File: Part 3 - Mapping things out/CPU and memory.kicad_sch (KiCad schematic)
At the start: 6 parts

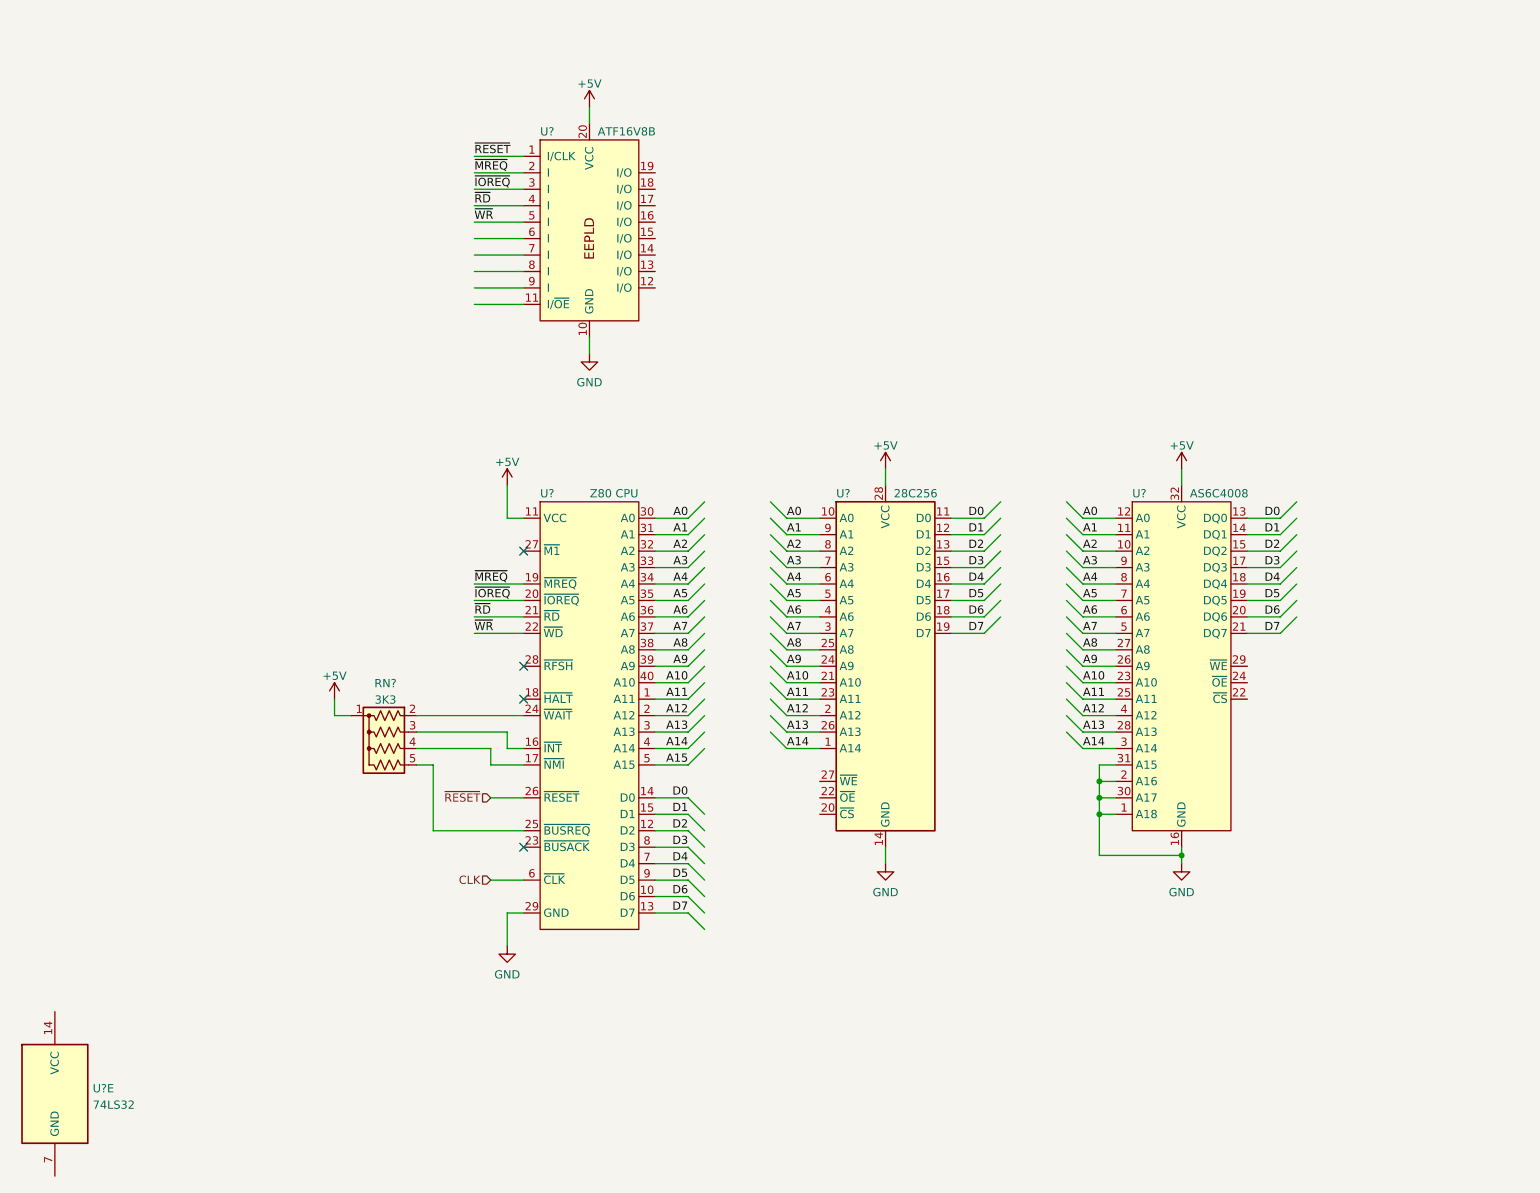
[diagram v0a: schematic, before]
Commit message: Updated glue logic and bank switching
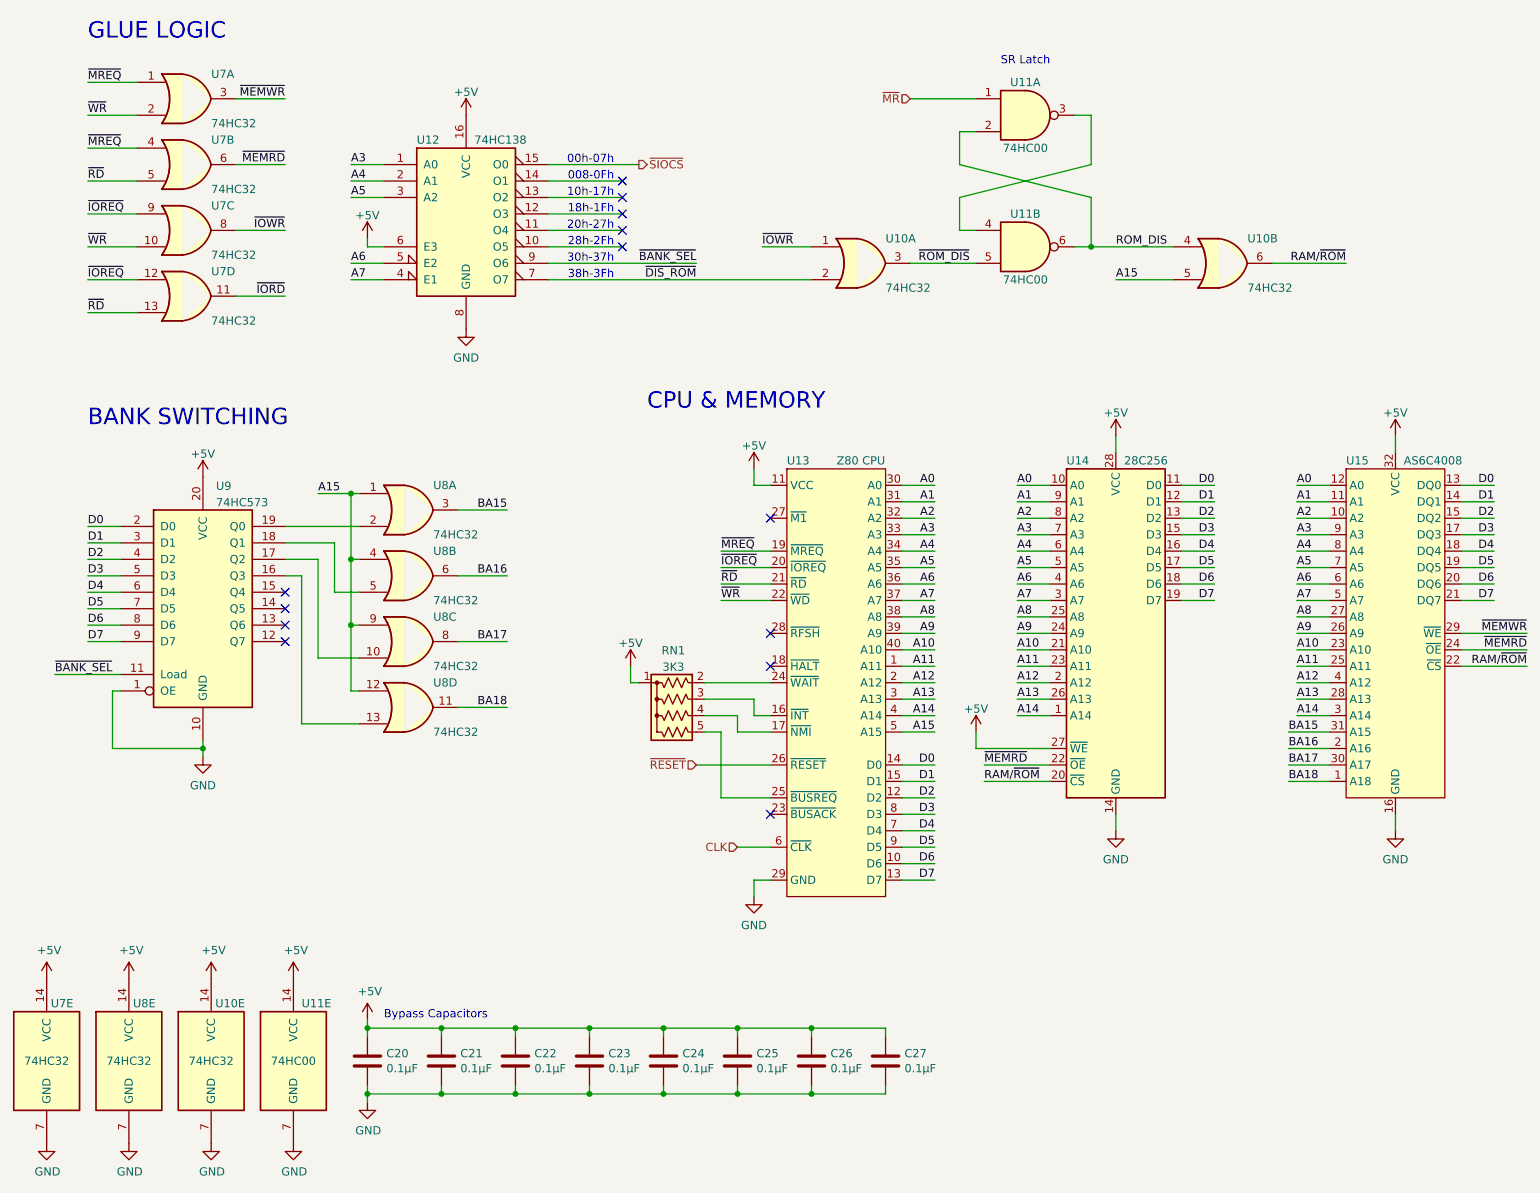
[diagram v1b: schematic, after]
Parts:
- removed U?: ATF16V8B, Package_DIP:DIP-20_W7.62mm_LongPads, symbol 0_Z80_Library:ATF16V8B
- added C20, C21, C22, C23, C24, C25, C26, C27: 0.1µF, Capacitor_THT:C_Disc_D3.0mm_W1.6mm_P2.50mm, symbol Device:C
- added U10, U8: 74HC32, symbol 74xx:74LS32
- added U11: 74HC00, symbol 74xx:74HC00
- added U12: 74HC138, symbol 74xx:74LS138
- added unit 1 of U7
- added unit 4 of U7
- added unit 3 of U7
- added unit 2 of U7
- added U9: 74HC573, symbol 74xx:74LS573
- U7: renamed from U?; value 74LS32 -> 74HC32
- gave numbers to parts that had none: 4
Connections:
- net +5V: now also U14.27 (~{WE}), U7.14 (VCC), C20.1, C21.1, C22.1, C23.1, C24.1, C25.1, C26.1, C27.1, U10.14 (VCC), U11.14 (VCC), U12.16 (VCC), U12.6 (E3), U8.14 (VCC), U9.20 (VCC)
- net A15: now also U10.5, U8.1, U8.12, U8.4, U8.9
- net A3: now also U12.1 (A0)
- net A4: now also U12.2 (A1)
- net A5: now also U12.3 (A2)
- net A6: now also U12.5 (E2)
- net A7: now also U12.4 (E1)
- net D0: now also U9.2 (D0)
- net D1: now also U9.3 (D1)
- net D2: now also U9.4 (D2)
- net D3: now also U9.5 (D3)
- net D4: now also U9.6 (D4)
- net D5: now also U9.7 (D5)
- net D6: now also U9.8 (D6)
- net D7: now also U9.9 (D7)
- net GND: now also U7.7 (GND), C20.2, C21.2, C22.2, C23.2, C24.2, C25.2, C26.2, C27.2, U10.7 (GND), U11.7 (GND), U12.8 (GND), U8.7 (GND), U9.1 (OE), U9.10 (GND); no longer U15.1 (A18), U15.2 (A16), U15.30 (A17), U15.31 (A15)
- net ~{IOREQ}: now also U7.12, U7.9
- net ~{MREQ}: now also U7.1, U7.4
- net ~{RD}: now also U7.13, U7.5
- net ~{WR}: now also U7.10, U7.2
- net RAM/~{ROM}: now reaches U15.22 (~{CS})
- net RAM/~{ROM}: now also U14.20 (~{CS}), U10.6
- net ~{MEMRD}: now reaches U15.24 (~{OE})
- net ~{MEMRD}: now also U14.22 (~{OE}), U7.6
- net ~{MEMWR}: now reaches U15.29 (~{WE})
- net ~{MEMWR}: now also U7.3
- new net: U11.3, U11.4
- new net: U8.13, U9.16 (Q3)
- new net: U8.10, U9.17 (Q2)
- new net: U8.5, U9.18 (Q1)
- new net: U8.2, U9.19 (Q0)
- new net BA15: U15.31 (A15), U8.3
- new net BA16: U15.2 (A16), U8.6
- new net BA17: U15.30 (A17), U8.8
- new net BA18: U15.1 (A18), U8.11
- new net ROM_DIS: U10.4, U11.2, U11.6
- new net ~{BANK_SEL}: U12.9 (O6), U9.11 (Load)
- new net ~{DIS_ROM}: U10.2, U12.7 (O7)
- new net ~{IORD}: U7.11
- new net ~{IOWR}: U10.1, U7.8
- new net ~{MR}: U11.1
- new net ~{ROM_DIS}: U10.3, U11.5
- new net ~{SIOCS}: U12.15 (O0)
- no-connect marks 4 -> 13
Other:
- note added: "008-0Fh"
- note added: "00h-07h"
- note added: "10h-17h"
- note added: "18h-1Fh"
- note added: "20h-27h"
- note added: "28h-2Fh"
- note added: "30h-37h"
- note added: "38h-3Fh"
- note added: "BANK SWITCHING"
- note added: "Bypass Capacitors"
- note added: "CPU & MEMORY"
- note added: "GLUE LOGIC"
- note added: "SR Latch"
- title: CPU, RAM, EEPROM & Logic -> CPU, EEPROM, RAM & basic logic
- moved on the sheet: RN1, U13, U14, U15, U7E
